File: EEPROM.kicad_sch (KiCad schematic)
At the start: 22 parts, among them IC1 PCA6408APW, IC2 AT24CS01, U2 TPS613221ADBVT

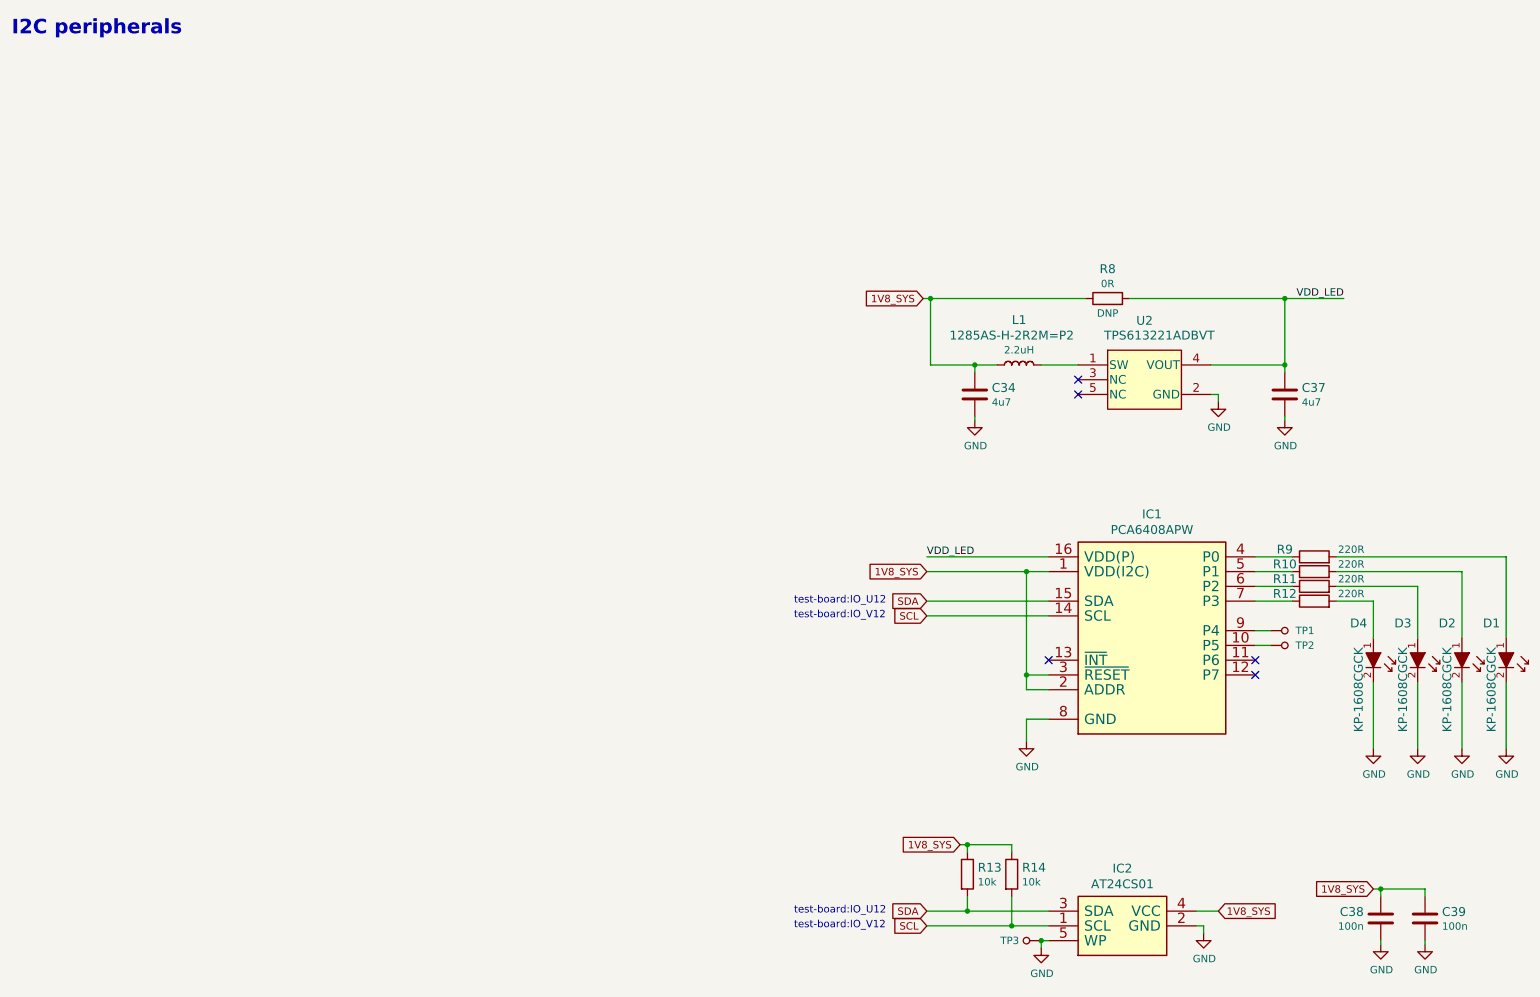
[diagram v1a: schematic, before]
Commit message: Introduce component standardization
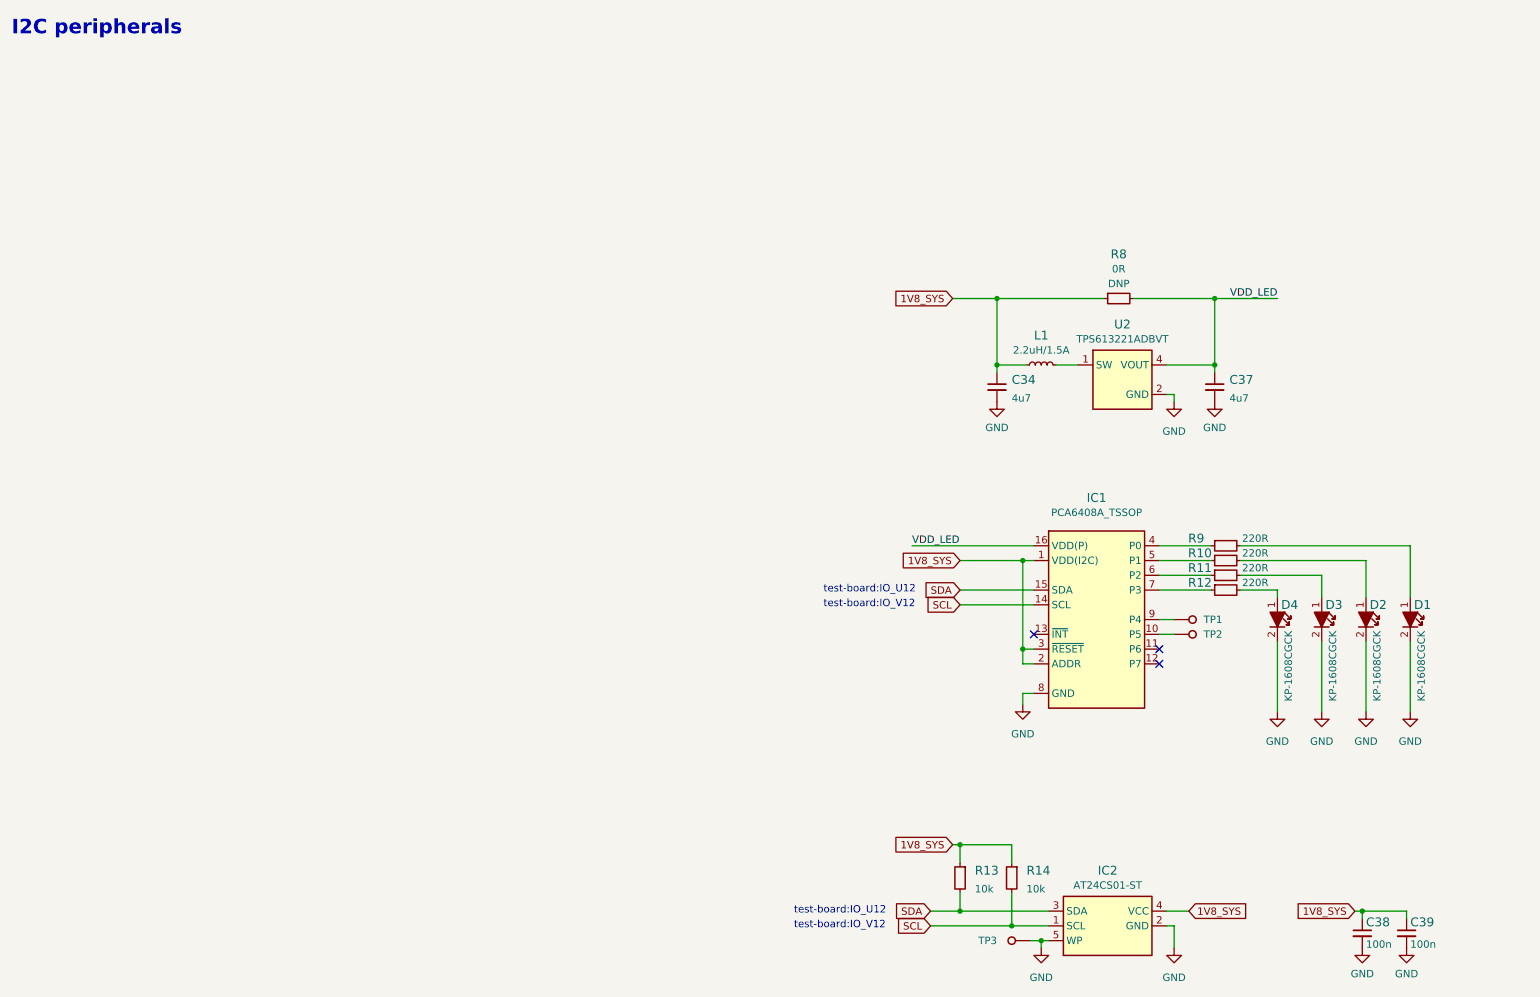
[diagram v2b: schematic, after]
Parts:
- C34, C37: footprint ddr5-testbed-footprints:0402-cap -> ddr5-testbed-footprints:C_0402_1005Metric; Author (none) -> Antmicro; License (none) -> Apache-2.0; Manufacturer MURATA -> Murata
- C38, C39: footprint ddr5-testbed-footprints:0402-cap -> ddr5-testbed-footprints:C_0402_1005Metric; Author (none) -> Antmicro; Dielectric (none) -> X5R; License (none) -> Apache-2.0; MPN 0402X104K6R3CT -> GRM155R61H104KE14D; Manufacturer Walsin -> Murata; Voltage (none) -> 50V
- D1, D2, D3, D4: value KP-1608CGCK -> LED_G_0603_KP-1608CGCK; footprint ddr5-testbed-footprints:LED_0603 -> ddr5-testbed-footprints:LED_0603_1608Metric_G; symbol ddr5-testbed:KP-1608CGCK -> ddr5-testbed:LED_G_0603_KP-1608CGCK; Author (none) -> Antmicro; License (none) -> Apache-2.0; Manufacturer KINGBRIGHT -> Kingbright
- IC1: value PCA6408APW -> PCA6408A_TSSOP; footprint ddr5-testbed-footprints:TSSOP-16 -> ddr5-testbed-footprints:TSSOP-16_4.4x5mm_P0.65mm; symbol ddr5-testbed:PCA6408APW -> ddr5-testbed:PCA6408A_TSSOP; Author (none) -> Antmicro; License (none) -> Apache-2.0
- IC2: value AT24CS01 -> AT24CS01_SOT23; symbol ddr5-testbed:AT24CS01-antmicroMemory -> ddr5-testbed:AT24CS01_SOT23; Author (none) -> Antmicro; License (none) -> Apache-2.0
- L1: value 1285AS-H-2R2M=P2 -> L_2.2u_1.5A_0806; footprint ddr5-testbed-footprints:0805-res -> ddr5-testbed-footprints:L_0806_2016Metric; symbol ddr5-testbed:1285AS-H-2R2M=P2 -> ddr5-testbed:L_2.2u_1.5A_0806; Author (none) -> Antmicro; License (none) -> Apache-2.0; Size (none) -> 2.0x1.6; Val 2.2uH -> 2.2uH/1.5A
- R10, R11, R12, R9: footprint ddr5-testbed-footprints:0402-res -> ddr5-testbed-footprints:R_0402_1005Metric; Author (none) -> Antmicro; License (none) -> Apache-2.0; MPN ERJ2GEJ221X -> CR0402-FX-2200GLF; Manufacturer Panasonic -> Bourns; Tolerance (none) -> 1%
- R13, R14: footprint ddr5-testbed-footprints:0402-res -> ddr5-testbed-footprints:R_0402_1005Metric; Author (none) -> Antmicro; License (none) -> Apache-2.0; MPN CRCW040210K0FKEDHP -> CR0402-FX-1002GLF; Manufacturer VISHAY -> Bourns; Tolerance (none) -> 1%
- R8: footprint ddr5-testbed-footprints:0402-res -> ddr5-testbed-footprints:R_0402_1005Metric; Author (none) -> Antmicro; Current (none) -> 1A; License (none) -> Apache-2.0; Manufacturer PANASONIC -> Panasonic
- TP1, TP2, TP3: value TP_SMD1MM -> TP_1mm_SMD; symbol ddr5-testbed:TP_SMD1MM -> ddr5-testbed:TP_1mm_SMD; Author (none) -> Antmicro; License (none) -> Apache-2.0
- U2: value TPS613221ADBVT -> TPS613221A_SOT-23-5; symbol ddr5-testbed:TPS613221ADBVT-antmicroDCDCConverters -> ddr5-testbed:TPS613221A_SOT-23-5; Author (none) -> Antmicro; License (none) -> Apache-2.0
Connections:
- no-connect marks 5 -> 3
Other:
- moved on the sheet: C34, C37, C38, C39, IC1, IC2, R10, R11, R12, R13, R14, R8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
